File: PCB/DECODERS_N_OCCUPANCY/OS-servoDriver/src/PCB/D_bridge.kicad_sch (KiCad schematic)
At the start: 5 parts

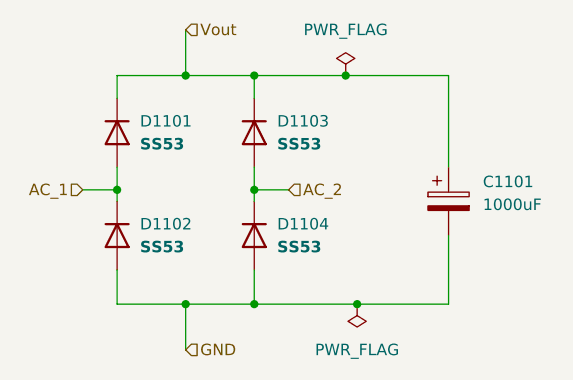
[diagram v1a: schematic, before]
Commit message: Added PDF files for all schematics
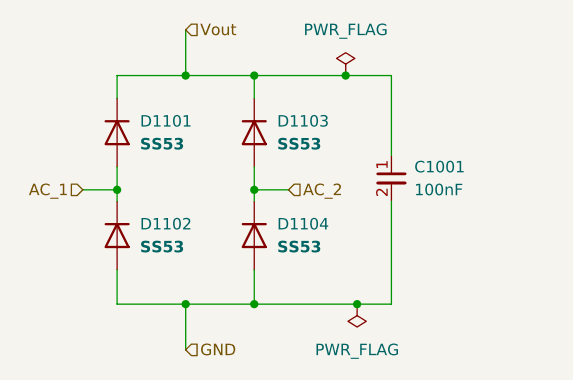
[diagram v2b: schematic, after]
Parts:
- removed C1101: 1000uF, Capacitor_SMD:CP_Elec_8x10.5, symbol Device:C_Polarized
- added C1001: 100nF, Capacitor_SMD:C_0603_1608Metric, symbol capacitor_miscellaneous:C_0603_100nF
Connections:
- net GND: now also C1001.2
- net Vout: now also C1001.1
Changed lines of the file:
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@@
 	(paper "A4")
+	(junction
+		(at 153.67 83.82)
+		(diameter 0)
+		(color 0 0 0 0)
+	)
 	(junction
 		(at 154.94 109.22)
@@
 	)
 	(junction
-		(at 153.67 83.82)
-		(diameter 0)
-		(color 0 0 0 0)
-	)
-	(junction
 		(at 143.51 83.82)
 		(diameter 0)
@@
 	(wire
 		(pts
-			(xy 165.1 83.82) (xy 153.67 83.82)
-		)
-		(stroke
-			(width 0)
-			(type default)
-		)
-	)
-	(wire
-		(pts
 			(xy 124.46 96.52) (xy 128.27 96.52)
 		)
@@
 	(wire
 		(pts
+			(xy 154.94 109.22) (xy 158.75 109.22)
+		)
+		(stroke
+			(width 0)
+			(type default)
+		)
+	)
+	(wire
+		(pts
 			(xy 128.27 96.52) (xy 128.27 97.79)
 		)
@@
 	(wire
 		(pts
-			(xy 165.1 109.22) (xy 165.1 101.6)
-		)
-		(stroke
-			(width 0)
-			(type default)
-		)
-	)
-	(wire
-		(pts
 			(xy 147.32 96.52) (xy 143.51 96.52)
 		)
@@
 	(wire
 		(pts
+			(xy 158.75 83.82) (xy 153.67 83.82)
+		)
+		(stroke
+			(width 0)
+			(type default)
+		)
+	)
+	(wire
+		(pts
 			(xy 135.89 78.74) (xy 135.89 83.82)
 		)
@@
 	(wire
 		(pts
+			(xy 158.75 92.71) (xy 158.75 83.82)
+		)
+		(stroke
+			(width 0)
+			(type default)
+		)
+	)
+	(wire
+		(pts
 			(xy 153.67 83.82) (xy 143.51 83.82)
 		)
@@
 	(wire
 		(pts
+			(xy 158.75 109.22) (xy 158.75 97.79)
+		)
+		(stroke
+			(width 0)
+			(type default)
+		)
+	)
+	(wire
+		(pts
 			(xy 143.51 105.41) (xy 143.51 109.22)
 		)
@@
 	(wire
 		(pts
-			(xy 154.94 109.22) (xy 165.1 109.22)
-		)
-		(stroke
-			(width 0)
-			(type default)
-		)
-	)
-	(wire
-		(pts
 			(xy 143.51 96.52) (xy 143.51 97.79)
 		)
@@
 		(pts
 			(xy 135.89 109.22) (xy 128.27 109.22)
-		)
-		(stroke
-			(width 0)
-			(type default)
-		)
-	)
-	(wire
-		(pts
-			(xy 165.1 93.98) (xy 165.1 83.82)
 		)
 		(stroke
@@
 	)
 	(symbol
+		(lib_id "capacitor_miscellaneous:C_0603_100nF")
+		(at 158.75 95.25 0)
+		(unit 1)
+		(exclude_from_sim no)
+		(in_bom yes)
+		(on_board yes)
+		(dnp no)
+		(fields_autoplaced yes)
+		(property "Reference" "C1001"
+			(at 161.29 93.9862 0)
+			(effects
+				(font
+					(size 1.27 1.27)
+				)
+				(justify left)
+			)
+		)
+		(property "Value" "100nF"
+			(at 161.29 96.5262 0)
+			(effects
+				(font
+					(size 1.27 1.27)
+				)
+				(justify left)
+			)
+		)
+		(property "Footprint" "Capacitor_SMD:C_0603_1608Metric"
+			(at 158.75 95.25 0)
+			(effects
+				(font
+					(size 1.27 1.27)
+				)
+				(hide yes)
+			)
+		)
+		(property "Datasheet" ""
+			(at 158.75 95.25 0)
+			(effects
+				(font
+					(size 1.27 1.27)
+				)
+				(hide yes)
+			)
+		)
+		(property "Description" ""
+			(at 158.75 95.25 0)
+			(effects
+				(font
+					(size 1.27 1.27)
+				)
+				(hide yes)
+			)
+		)
+		(property "JLCPCB Part#" "C14663"
+			(at 158.75 95.25 0)
+			(effects
+				(font
+					(size 1.27 1.27)
+				)
+				(hide yes)
+			)
+		)
+		(pin "1"
+		)
+		(pin "2"
+		)
+		(instances
+			(project "OS-servoDriver"
+				(path "/b6ccf16f-5cc5-4d5a-97fc-20f76ee5c73e/0c27c8b7-3734-4129-8cd0-d3d033ef2608"
+					(reference "C1001")
+					(unit 1)
+				)
+			)
+		)
+	)
+	(symbol
 		(lib_id "power:PWR_FLAG")
 		(at 153.67 83.82 0)
@@
 					(unit 1)
 				)
-			)
-		)
-	)
-	(symbol
-		(lib_id "Device:C_Polarized")
-		(at 165.1 97.79 0)
-		(unit 1)
-		(exclude_from_sim no)
-		(in_bom yes)
-		(on_board yes)
-		(dnp no)
-		(fields_autoplaced yes)
-		(property "Reference" "C1101"
-			(at 168.91 95.631 0)
-			(effects
-				(font
-					(size 1.27 1.27)
-				)
-				(justify left)
-			)
-		)
-		(property "Value" "1000uF"
-			(at 168.91 98.171 0)
-			(effects
-				(font
-					(size 1.27 1.27)
-				)
-				(justify left)
-			)
-		)
-		(property "Footprint" "Capacitor_SMD:CP_Elec_8x10.5"
-			(at 166.0652 101.6 0)
-			(effects
-				(font
-					(size 1.27 1.27)
-				)
-				(hide yes)
-			)
-		)
-		(property "Datasheet" "~"
-			(at 165.1 97.79 0)
-			(effects
-				(font
-					(size 1.27 1.27)
-				)
-				(hide yes)
-			)
-		)
-		(property "Description" ""
-			(at 165.1 97.79 0)
-			(effects
-				(font
-					(size 1.27 1.27)
-				)
-				(hide yes)
-			)
-		)
-		(property "JLCPCB Part#" "C5162347"
-			(at 165.1 97.79 0)
-			(effects
-				(font
-					(size 1.27 1.27)
-				)
-				(hide yes)
-			)
-		)
-		(pin "1"
-		)
-		(pin "2"
-		)
-		(instances
-			(project "OS-servoDriver"
-				(path "/b6ccf16f-5cc5-4d5a-97fc-20f76ee5c73e/0c27c8b7-3734-4129-8cd0-d3d033ef2608"
-					(reference "C1101")
-					(unit 1)
-				)
